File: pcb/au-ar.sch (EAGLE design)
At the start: 55 parts, among them U1 TPD12S016PWR, U2 TPD12S016PWR

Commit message: almost done routing
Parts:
- added C4, C5: 0.1uF, rcl:C-USC0603
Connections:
- net 3V3: now also C4.1, C5.1
- net GND: now also C4.2, C5.2
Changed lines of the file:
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@@
 <?xml version="1.0" encoding="utf-8"?>
 <!DOCTYPE eagle SYSTEM "eagle.dtd">
-<eagle version="9.4.0">
+<eagle version="9.3.1">
 <drawing>
 <settings>
@@
 <part name="C2" library="rcl" library_urn="urn:adsk.eagle:library:334" deviceset="C-US" device="C0603" package3d_urn="urn:adsk.eagle:package:23616/2" value="0.1uF"/>
 <part name="C3" library="rcl" library_urn="urn:adsk.eagle:library:334" deviceset="C-US" device="C0603" package3d_urn="urn:adsk.eagle:package:23616/2" value="0.1uF"/>
+<part name="C4" library="rcl" library_urn="urn:adsk.eagle:library:334" deviceset="C-US" device="C0603" package3d_urn="urn:adsk.eagle:package:23616/2" value="0.1uF"/>
+<part name="C5" library="rcl" library_urn="urn:adsk.eagle:library:334" deviceset="C-US" device="C0603" package3d_urn="urn:adsk.eagle:package:23616/2" value="0.1uF"/>
 </parts>
 <sheets>
@@
 <attribute name="VALUE" x="-1.524" y="46.609" size="1.778" layer="96"/>
 </instance>
+<instance part="C4" gate="G$1" x="99.06" y="76.2" smashed="yes">
+<attribute name="NAME" x="100.076" y="76.835" size="1.778" layer="95"/>
+<attribute name="VALUE" x="100.076" y="72.009" size="1.778" layer="96"/>
+</instance>
+<instance part="C5" gate="G$1" x="210.82" y="78.74" smashed="yes">
+<attribute name="NAME" x="211.836" y="79.375" size="1.778" layer="95"/>
+<attribute name="VALUE" x="211.836" y="74.549" size="1.778" layer="96"/>
+</instance>
 </instances>
 <busses>
@@
 <pinref part="C2" gate="G$1" pin="2"/>
 <wire x1="106.68" y1="48.26" x2="106.68" y2="43.18" width="0.1524" layer="91"/>
-<wire x1="106.68" y1="43.18" x2="-2.54" y2="43.18" width="0.1524" layer="91"/>
+<wire x1="106.68" y1="43.18" x2="99.06" y2="43.18" width="0.1524" layer="91"/>
 <junction x="-2.54" y="43.18"/>
+<pinref part="C4" gate="G$1" pin="2"/>
+<wire x1="99.06" y1="43.18" x2="-2.54" y2="43.18" width="0.1524" layer="91"/>
+<wire x1="99.06" y1="71.12" x2="99.06" y2="43.18" width="0.1524" layer="91"/>
+<junction x="99.06" y="43.18"/>
 </segment>
 <segment>
@@
 <segment>
 <pinref part="U2" gate="A" pin="GND_3"/>
-<wire x1="190.5" y1="58.42" x2="200.66" y2="58.42" width="0.1524" layer="91"/>
 <label x="200.66" y="58.42" size="1.778" layer="95"/>
+<pinref part="C5" gate="G$1" pin="2"/>
+<wire x1="210.82" y1="73.66" x2="210.82" y2="58.42" width="0.1524" layer="91"/>
+<wire x1="210.82" y1="58.42" x2="190.5" y2="58.42" width="0.1524" layer="91"/>
 </segment>
 </net>
@@
 <wire x1="91.44" y1="81.28" x2="91.44" y2="88.9" width="0.1524" layer="91"/>
 <label x="91.44" y="88.9" size="1.778" layer="95"/>
+<pinref part="C4" gate="G$1" pin="1"/>
+<wire x1="91.44" y1="81.28" x2="99.06" y2="81.28" width="0.1524" layer="91"/>
+<wire x1="99.06" y1="81.28" x2="99.06" y2="78.74" width="0.1524" layer="91"/>
+<junction x="91.44" y="81.28"/>
 </segment>
 <segment>
@@
 <wire x1="203.2" y1="83.82" x2="203.2" y2="93.98" width="0.1524" layer="91"/>
 <label x="203.2" y="93.98" size="1.778" layer="95"/>
-</segment>
-</net>
+<pinref part="C5" gate="G$1" pin="1"/>
+<wire x1="203.2" y1="83.82" x2="210.82" y2="83.82" width="0.1524" layer="91"/>
+<wire x1="210.82" y1="83.82" x2="210.82" y2="81.28" width="0.1524" layer="91"/>
+<junction x="203.2" y="83.82"/>
+</segment>
+</net>

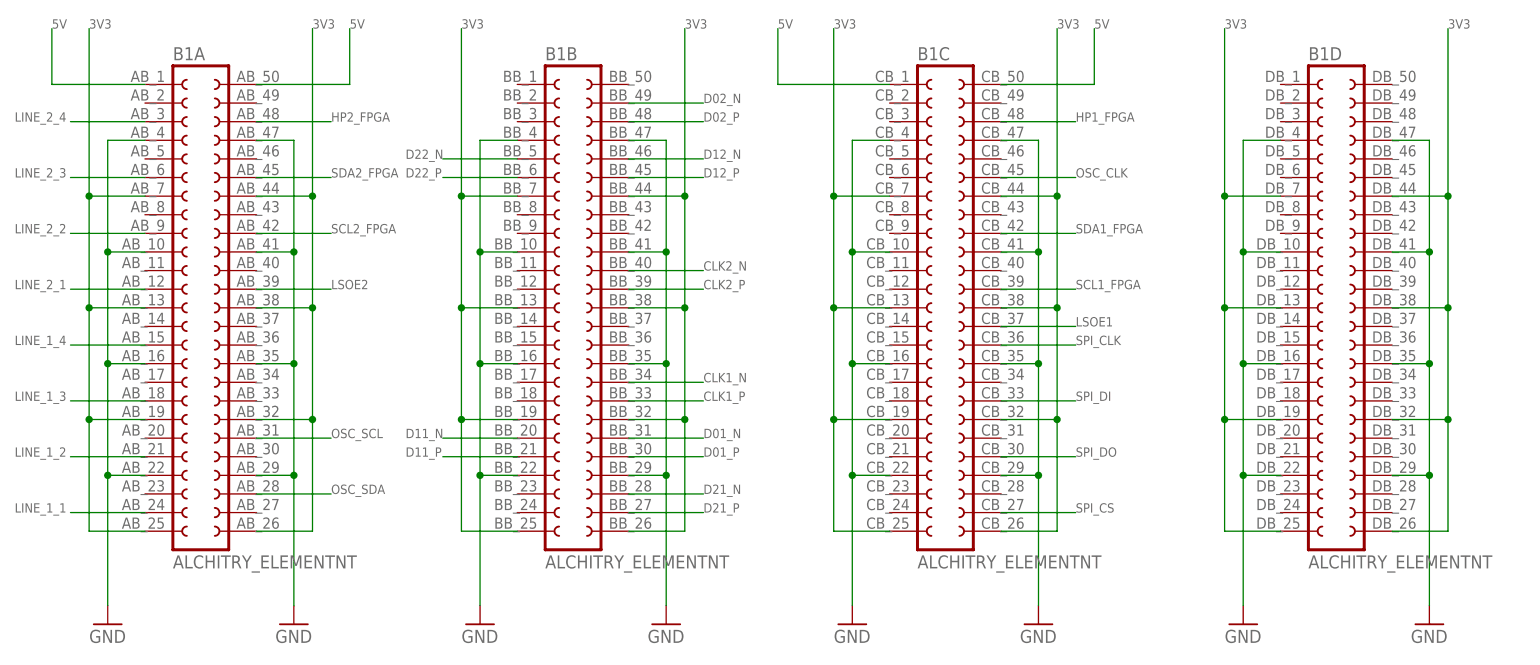
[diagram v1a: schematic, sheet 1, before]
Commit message: need to add mosfet and order
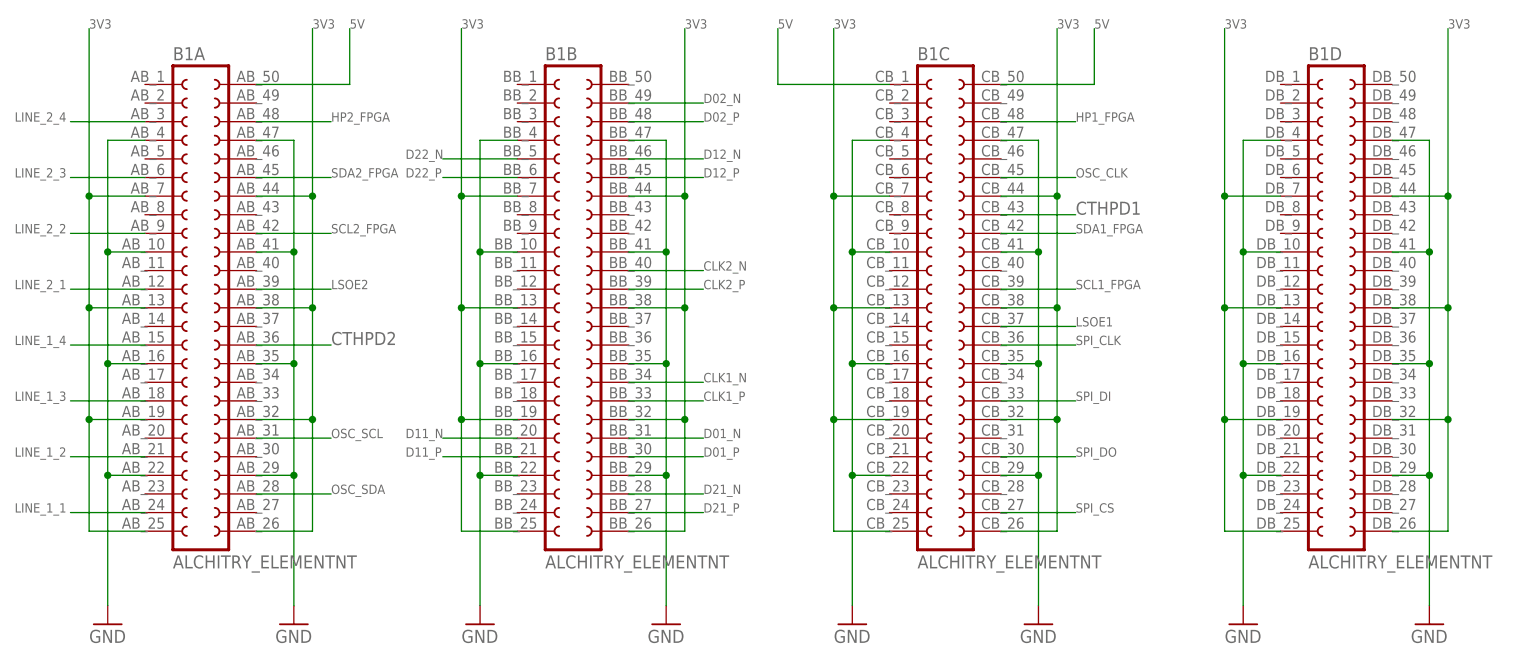
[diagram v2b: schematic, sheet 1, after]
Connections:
- net 5V: no longer B1A.1
- net CTHPD1: now also B1C.43
- net CTHPD2: now also B1A.36
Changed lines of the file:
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@@
 <net name="5V" class="0">
-<segment>
-<pinref part="B1" gate="A" pin="1"/>
-<wire x1="33.02" y1="91.44" x2="20.32" y2="91.44" width="0.1524" layer="91"/>
-<wire x1="20.32" y1="91.44" x2="20.32" y2="99.06" width="0.1524" layer="91"/>
-<label x="20.32" y="99.06" size="1.27" layer="95"/>
-</segment>
 <segment>
 <pinref part="B1" gate="A" pin="50"/>
@@
 </segment>
 </net>
+<net name="CTHPD1" class="0">
+<segment>
+<pinref part="B1" gate="C" pin="43"/>
+<wire x1="149.86" y1="73.66" x2="160.02" y2="73.66" width="0.1524" layer="91"/>
+<label x="160.02" y="73.66" size="1.778" layer="95"/>
+</segment>
+</net>
+<net name="CTHPD2" class="0">
+<segment>
+<pinref part="B1" gate="A" pin="36"/>
+<wire x1="48.26" y1="55.88" x2="58.42" y2="55.88" width="0.1524" layer="91"/>
+<label x="58.42" y="55.88" size="1.778" layer="95"/>
+</segment>
+</net>

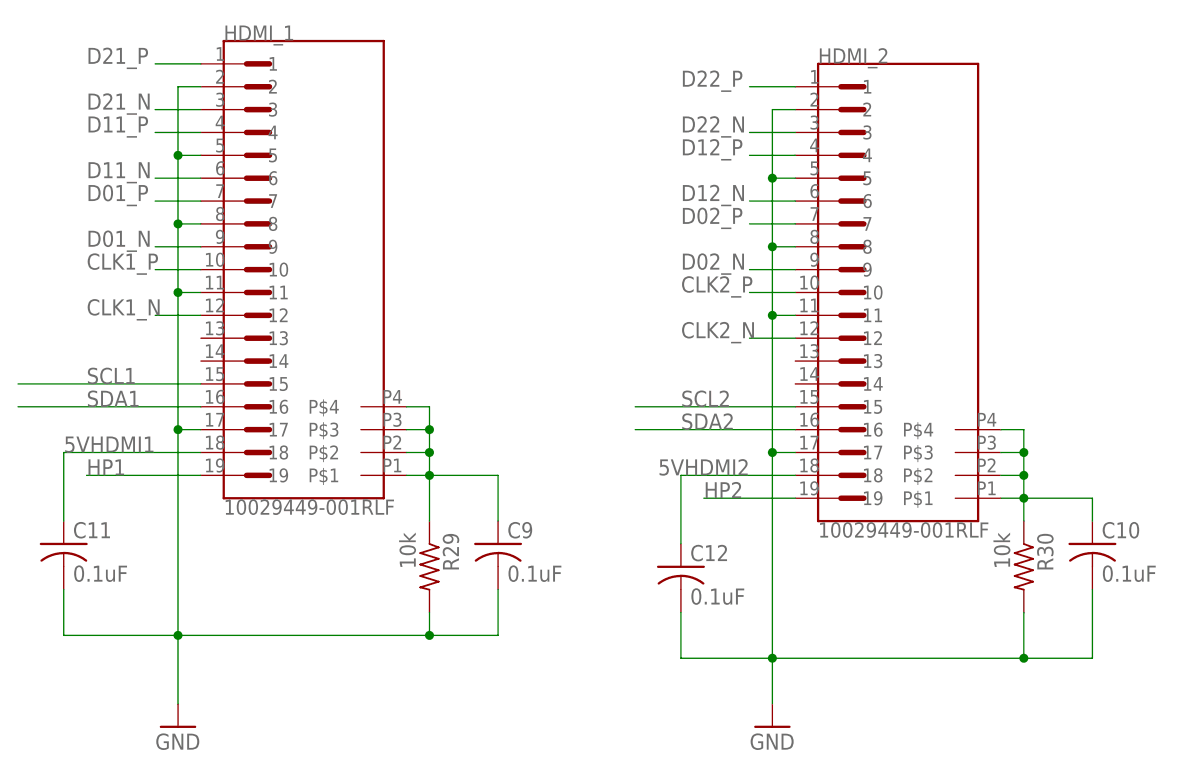
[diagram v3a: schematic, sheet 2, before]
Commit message: added partslist and solder jumper for hdmi input, labeled hdmi input and output added up to date gerbers.
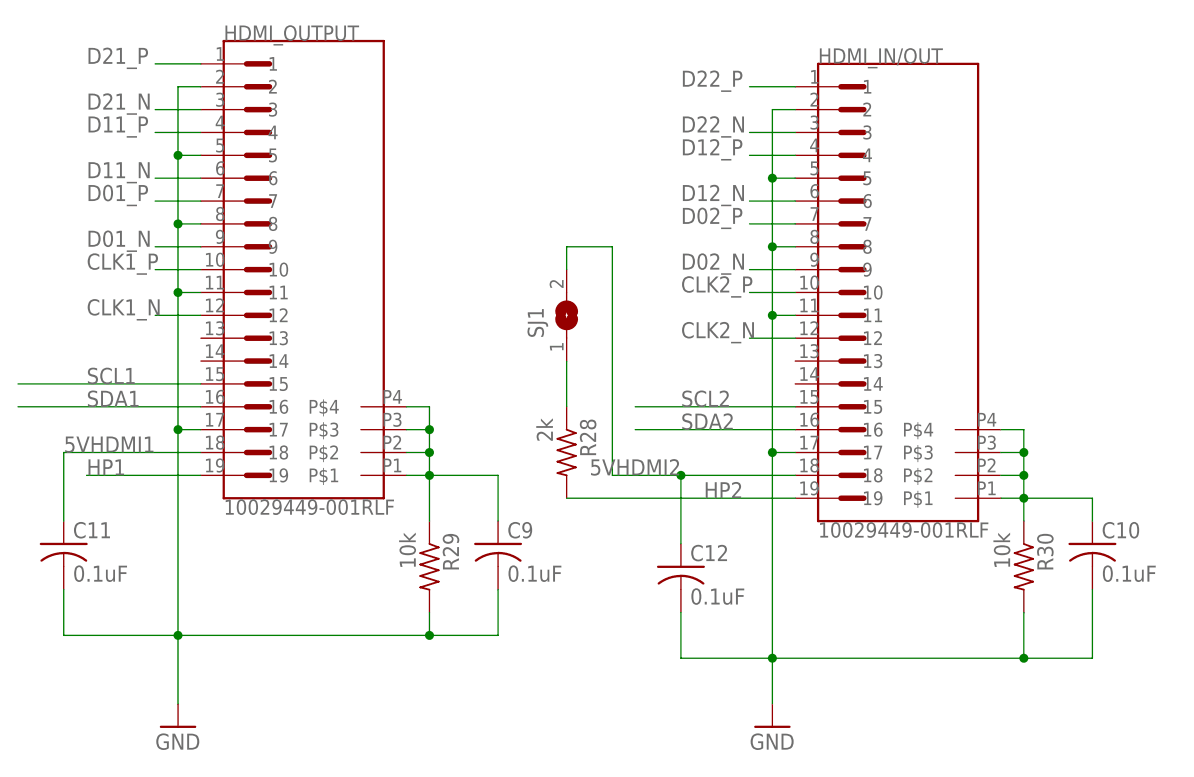
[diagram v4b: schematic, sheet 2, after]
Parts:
- added R28: 2k, rcl:R-US_R0603
- added SJ1: (no value), jumper:SJ
- R1, R10, R11, R12, R13, R14, R15, R16, R17, R18, R19, R2, R20, R21, R22, R23, R24, R25, R26, R3, R4, R7, R8, R9: value (none) -> DNP
- renumbered HDMI_1 to HDMI_OUTPUT, HDMI_2 to HDMI_IN/OUT
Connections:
- new net N$2: R28.1, SJ1.1
- net 5VHDMI2: now also SJ1.2
- net HP2: now also R28.2

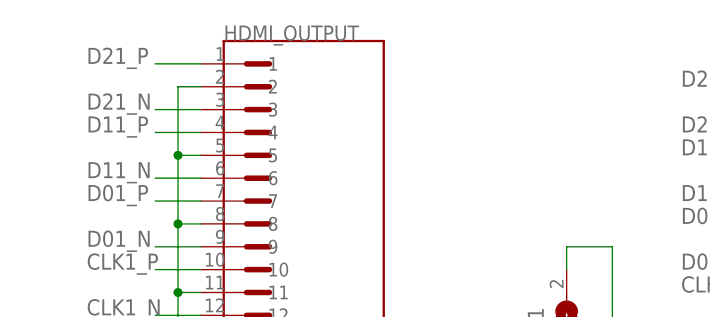
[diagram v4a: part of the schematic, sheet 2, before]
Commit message: hdmi ground vias moved
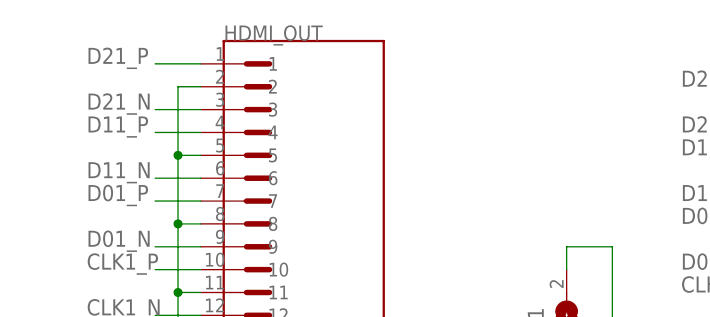
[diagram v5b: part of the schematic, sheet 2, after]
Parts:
- renumbered HDMI_OUTPUT to HDMI_OUT
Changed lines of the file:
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@@
 <?xml version="1.0" encoding="utf-8"?>
 <!DOCTYPE eagle SYSTEM "eagle.dtd">
-<eagle version="9.4.0">
+<eagle version="9.5.0">
 <drawing>
 <settings>
@@
 <parts>
 <part name="B1" library="alchitry_elements" deviceset="ALCHITRY_ELEMENT" device="NT"/>
-<part name="HDMI_OUTPUT" library="10029449-001RLF" deviceset="10029449-001RLF" device=""/>
+<part name="HDMI_OUT" library="10029449-001RLF" deviceset="10029449-001RLF" device=""/>
 <part name="HDMI_IN/OUT" library="10029449-001RLF" deviceset="10029449-001RLF" device=""/>
 <part name="GND3" library="supply1" library_urn="urn:adsk.eagle:library:371" deviceset="GND" device=""/>
@@
 </plain>
 <instances>
-<instance part="HDMI_OUTPUT" gate="G$1" x="33.02" y="68.58" smashed="yes">
+<instance part="HDMI_OUT" gate="G$1" x="33.02" y="68.58" smashed="yes">
 <attribute name="NAME" x="27.931240625" y="94.0238" size="1.679290625" layer="95"/>
 <attribute name="VALUE" x="27.92996875" y="41.3483" size="1.679709375" layer="96"/>
@@
 <net name="D21_P" class="1">
 <segment>
-<pinref part="HDMI_OUTPUT" gate="G$1" pin="1"/>
+<pinref part="HDMI_OUT" gate="G$1" pin="1"/>
 <wire x1="25.4" y1="91.44" x2="20.32" y2="91.44" width="0.1524" layer="91"/>
 <label x="12.7" y="91.44" size="1.778" layer="95"/>
@@
 <net name="D21_N" class="1">
 <segment>
-<pinref part="HDMI_OUTPUT" gate="G$1" pin="3"/>
+<pinref part="HDMI_OUT" gate="G$1" pin="3"/>
 <wire x1="25.4" y1="86.36" x2="20.32" y2="86.36" width="0.1524" layer="91"/>
 <label x="12.7" y="86.36" size="1.778" layer="95"/>
@@
 <net name="D11_P" class="1">
 <segment>
-<pinref part="HDMI_OUTPUT" gate="G$1" pin="4"/>
+<pinref part="HDMI_OUT" gate="G$1" pin="4"/>
 <wire x1="25.4" y1="83.82" x2="20.32" y2="83.82" width="0.1524" layer="91"/>
 <label x="12.7" y="83.82" size="1.778" layer="95"/>
@@
 <net name="D11_N" class="1">
 <segment>
-<pinref part="HDMI_OUTPUT" gate="G$1" pin="6"/>
+<pinref part="HDMI_OUT" gate="G$1" pin="6"/>
 <wire x1="25.4" y1="78.74" x2="20.32" y2="78.74" width="0.1524" layer="91"/>
 <label x="12.7" y="78.74" size="1.778" layer="95"/>
@@
 <net name="D01_P" class="1">
 <segment>
-<pinref part="HDMI_OUTPUT" gate="G$1" pin="7"/>
+<pinref part="HDMI_OUT" gate="G$1" pin="7"/>
 <wire x1="25.4" y1="76.2" x2="20.32" y2="76.2" width="0.1524" layer="91"/>
 <label x="12.7" y="76.2" size="1.778" layer="95"/>
@@
 <net name="D01_N" class="1">
 <segment>
-<pinref part="HDMI_OUTPUT" gate="G$1" pin="9"/>
+<pinref part="HDMI_OUT" gate="G$1" pin="9"/>
 <wire x1="25.4" y1="71.12" x2="20.32" y2="71.12" width="0.1524" layer="91"/>
 <label x="12.7" y="71.12" size="1.778" layer="95"/>
@@
 <net name="CLK1_P" class="1">
 <segment>
-<pinref part="HDMI_OUTPUT" gate="G$1" pin="10"/>
+<pinref part="HDMI_OUT" gate="G$1" pin="10"/>
 <wire x1="25.4" y1="68.58" x2="20.32" y2="68.58" width="0.1524" layer="91"/>
 <label x="12.7" y="68.58" size="1.778" layer="95"/>
@@
 <net name="CLK1_N" class="1">
 <segment>
-<pinref part="HDMI_OUTPUT" gate="G$1" pin="12"/>
+<pinref part="HDMI_OUT" gate="G$1" pin="12"/>
 <wire x1="25.4" y1="63.5" x2="20.32" y2="63.5" width="0.1524" layer="91"/>
 <label x="12.7" y="63.5" size="1.778" layer="95"/>
@@
 <net name="SCL1" class="0">
 <segment>
-<pinref part="HDMI_OUTPUT" gate="G$1" pin="15"/>
+<pinref part="HDMI_OUT" gate="G$1" pin="15"/>
 <label x="12.7" y="55.88" size="1.778" layer="95"/>
 <wire x1="25.4" y1="55.88" x2="5.08" y2="55.88" width="0.1524" layer="91"/>
@@
 <net name="SDA1" class="0">
 <segment>
-<pinref part="HDMI_OUTPUT" gate="G$1" pin="16"/>
+<pinref part="HDMI_OUT" gate="G$1" pin="16"/>
 <label x="12.7" y="53.34" size="1.778" layer="95"/>
 <wire x1="25.4" y1="53.34" x2="5.08" y2="53.34" width="0.1524" layer="91"/>
@@
 <net name="5VHDMI1" class="0">
 <segment>
-<pinref part="HDMI_OUTPUT" gate="G$1" pin="18"/>
+<pinref part="HDMI_OUT" gate="G$1" pin="18"/>
 <label x="10.16" y="48.26" size="1.778" layer="95"/>
 <wire x1="25.4" y1="48.26" x2="10.16" y2="48.26" width="0.1524" layer="91"/>
@@
 <net name="HP1" class="0">
 <segment>
-<pinref part="HDMI_OUTPUT" gate="G$1" pin="19"/>
+<pinref part="HDMI_OUT" gate="G$1" pin="19"/>
 <label x="12.7" y="45.72" size="1.778" layer="95"/>
 <wire x1="25.4" y1="45.72" x2="12.7" y2="45.72" width="0.1524" layer="91"/>
@@
 <net name="GND" class="0">
 <segment>
-<pinref part="HDMI_OUTPUT" gate="G$1" pin="2"/>
+<pinref part="HDMI_OUT" gate="G$1" pin="2"/>
 <wire x1="25.4" y1="88.9" x2="22.86" y2="88.9" width="0.1524" layer="91"/>
-<pinref part="HDMI_OUTPUT" gate="G$1" pin="5"/>
+<pinref part="HDMI_OUT" gate="G$1" pin="5"/>
 <wire x1="25.4" y1="81.28" x2="22.86" y2="81.28" width="0.1524" layer="91"/>
 <wire x1="22.86" y1="88.9" x2="22.86" y2="81.28" width="0.1524" layer="91"/>
 <junction x="22.86" y="81.28"/>
-<pinref part="HDMI_OUTPUT" gate="G$1" pin="8"/>
+<pinref part="HDMI_OUT" gate="G$1" pin="8"/>
 <wire x1="25.4" y1="73.66" x2="22.86" y2="73.66" width="0.1524" layer="91"/>
 <wire x1="22.86" y1="81.28" x2="22.86" y2="73.66" width="0.1524" layer="91"/>
 <junction x="22.86" y="73.66"/>
-<pinref part="HDMI_OUTPUT" gate="G$1" pin="11"/>
+<pinref part="HDMI_OUT" gate="G$1" pin="11"/>
 <wire x1="25.4" y1="66.04" x2="22.86" y2="66.04" width="0.1524" layer="91"/>
 <wire x1="22.86" y1="73.66" x2="22.86" y2="66.04" width="0.1524" layer="91"/>
 <junction x="22.86" y="66.04"/>
-<pinref part="HDMI_OUTPUT" gate="G$1" pin="17"/>
+<pinref part="HDMI_OUT" gate="G$1" pin="17"/>
 <wire x1="25.4" y1="50.8" x2="22.86" y2="50.8" width="0.1524" layer="91"/>
 <wire x1="22.86" y1="66.04" x2="22.86" y2="50.8" width="0.1524" layer="91"/>
@@
 <net name="N$13" class="0">
 <segment>
-<pinref part="HDMI_OUTPUT" gate="G$1" pin="P$4"/>
+<pinref part="HDMI_OUT" gate="G$1" pin="P$4"/>
 <wire x1="48.26" y1="53.34" x2="50.8" y2="53.34" width="0.1524" layer="91"/>
 <wire x1="50.8" y1="53.34" x2="50.8" y2="50.8" width="0.1524" layer="91"/>
-<pinref part="HDMI_OUTPUT" gate="G$1" pin="P$3"/>
+<pinref part="HDMI_OUT" gate="G$1" pin="P$3"/>
 <wire x1="50.8" y1="50.8" x2="48.26" y2="50.8" width="0.1524" layer="91"/>
-<pinref part="HDMI_OUTPUT" gate="G$1" pin="P$2"/>
+<pinref part="HDMI_OUT" gate="G$1" pin="P$2"/>
 <wire x1="48.26" y1="48.26" x2="50.8" y2="48.26" width="0.1524" layer="91"/>
 <wire x1="50.8" y1="48.26" x2="50.8" y2="45.72" width="0.1524" layer="91"/>
-<pinref part="HDMI_OUTPUT" gate="G$1" pin="P$1"/>
+<pinref part="HDMI_OUT" gate="G$1" pin="P$1"/>
 <wire x1="50.8" y1="45.72" x2="48.26" y2="45.72" width="0.1524" layer="91"/>
 <wire x1="50.8" y1="50.8" x2="50.8" y2="48.26" width="0.1524" layer="91"/>
